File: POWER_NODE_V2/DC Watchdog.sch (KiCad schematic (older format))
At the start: 0 parts

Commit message: Power Node V2 WIP
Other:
- note added: "TODO: Connector, ESD protection"
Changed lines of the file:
@@
 Text HLabel 3200 2800 0    60   Input ~ 0
 DC_WATCHDOG
+Text Notes 4850 2750 0    60   ~ 0
+TODO: Connector, ESD protection
 $EndSCHEMATC

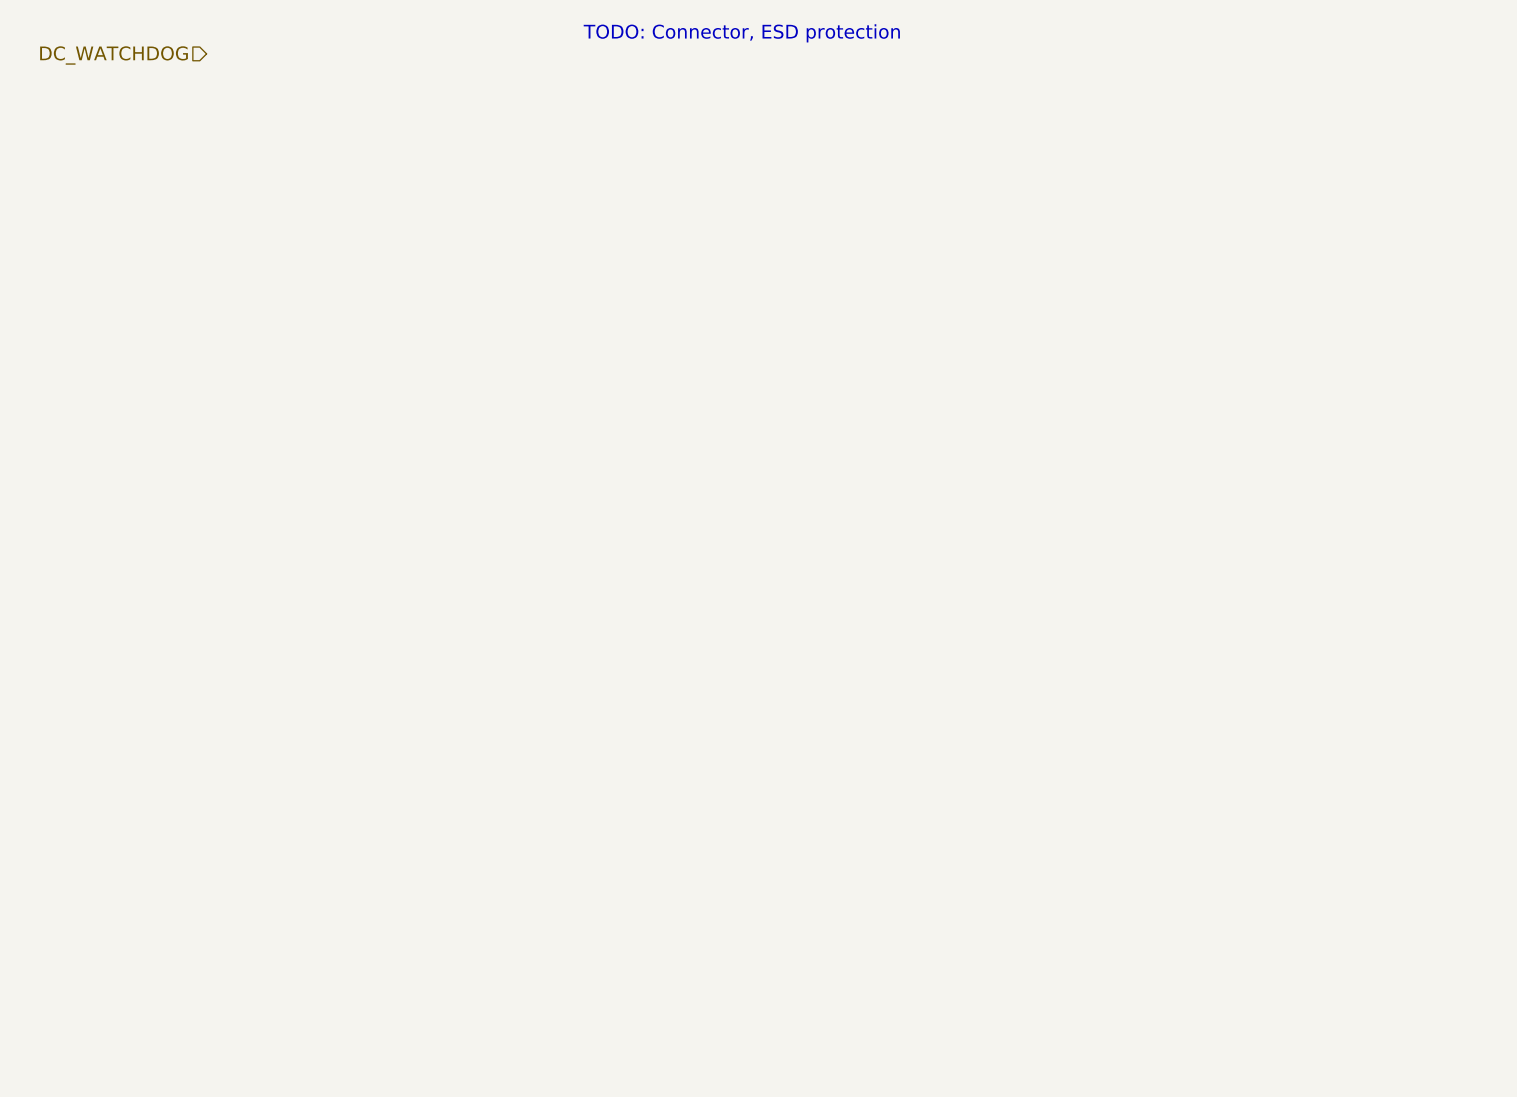
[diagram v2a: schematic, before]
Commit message: Schematic for Power Node V2 mostly done - mostly need connectors
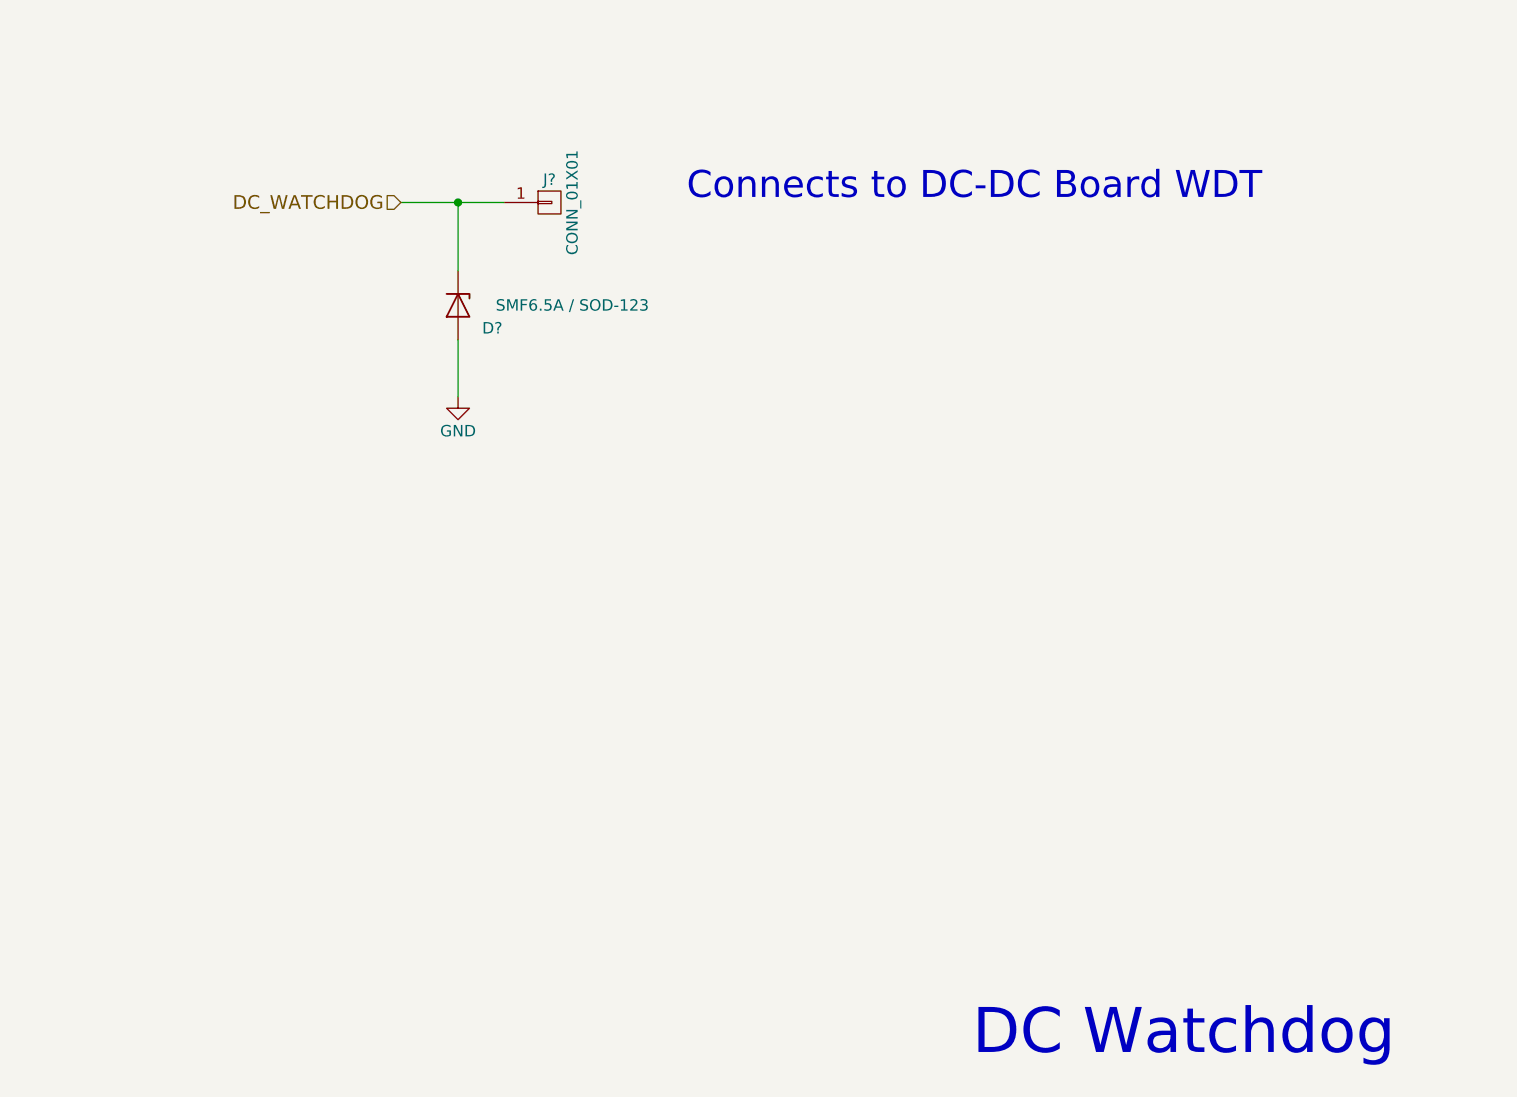
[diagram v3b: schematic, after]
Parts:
- added D?: SMF6.5A / SOD-123, symbol D_Zener
- added J?: CONN_01X01, symbol CONN_01X01
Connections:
- net DC_WATCHDOG: now also D?.1 (K), J?.1 (P1)
- new net GND: D?.2 (A)
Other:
- note added: "Connects to DC-DC Board WDT"
- note added: "DC Watchdog"
- note removed: "TODO: Connector, ESD protection"
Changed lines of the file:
@@
 EELAYER 25 0
 EELAYER END
-$Descr A4 11693 8268
+$Descr USLetter 11000 8500
 encoding utf-8
-Sheet 6 8
+Sheet 6 9
 Title ""
 Date ""
@@
 Comment4 ""
 $EndDescr
-Text HLabel 3200 2800 0    60   Input ~ 0
+Text HLabel 4050 3450 0    60   Input ~ 0
 DC_WATCHDOG
-Text Notes 4850 2750 0    60   ~ 0
-TODO: Connector, ESD protection
+$Comp
+L CONN_01X01 J?
+U 1 1 5951AEA4
+P 4700 3450
+F 0 "J?" H 4700 3550 50  0000 C CNN
+F 1 "CONN_01X01" V 4800 3450 50  0000 C CNN
+F 2 "" H 4700 3450 50  0001 C CNN
+F 3 "" H 4700 3450 50  0001 C CNN
+	1    4700 3450
+	1    0    0    -1
+$EndComp
+Wire Wire Line
+	4050 3450 4500 3450
+$Comp
+L D_Zener D?
+U 1 1 5952660A
+P 4300 3900
+F 0 "D?" V 4400 4050 50  0000 C CNN
+F 1 "SMF6.5A / SOD-123" V 4300 4400 50  0000 C CNN
+F 2 "" H 4300 3900 50  0001 C CNN
+F 3 "" H 4300 3900 50  0001 C CNN
+	1    4300 3900
+	0    1    1    0
+$EndComp
+Wire Wire Line
+	4300 3750 4300 3450
+Connection ~ 4300 3450
+$Comp
+L GND #PWR?
+U 1 1 5952668C
+P 4300 4300
+F 0 "#PWR?" H 4300 4050 50  0001 C CNN
+F 1 "GND" H 4300 4150 50  0000 C CNN
+F 2 "" H 4300 4300 50  0001 C CNN
+F 3 "" H 4300 4300 50  0001 C CNN
+	1    4300 4300
+	1    0    0    -1
+$EndComp
+Wire Wire Line
+	4300 4300 4300 4050
+Text Notes 5300 3450 0    118  ~ 0
+Connects to DC-DC Board WDT
+Text Notes 6550 7200 0    197  ~ 0
+DC Watchdog
 $EndSCHEMATC

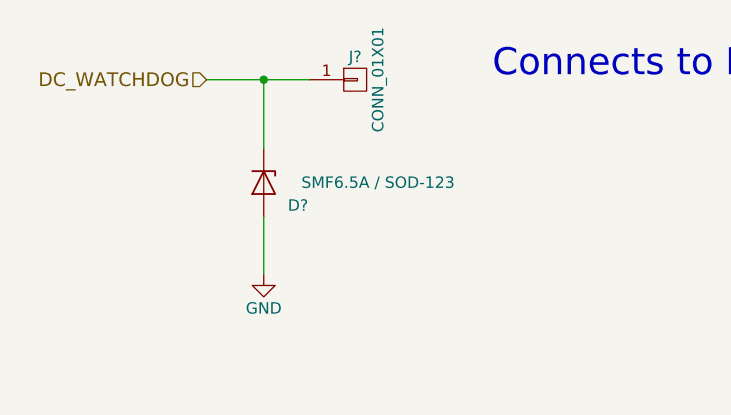
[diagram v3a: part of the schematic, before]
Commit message: made a lot of footprints, began PCB layout for power node v2
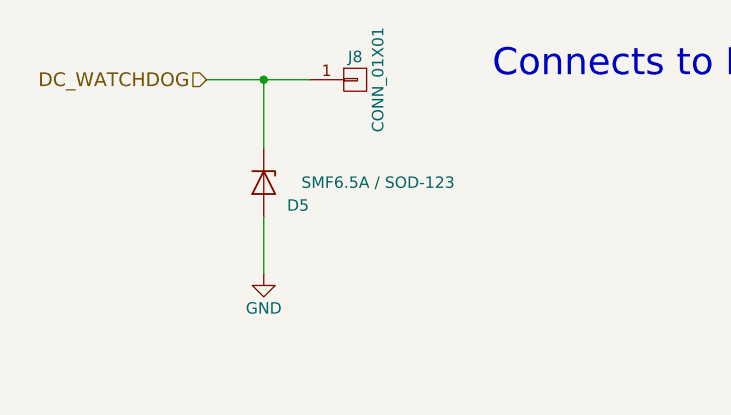
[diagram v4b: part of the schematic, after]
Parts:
- D5: renamed from D?; footprint (none) -> Diodes_SMD:D_SOD-123
- J8: renamed from J?; footprint (none) -> Pin_Headers:Pin_Header_Straight_1x01_Pitch2.54mm
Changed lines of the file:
@@
 DC_WATCHDOG
 $Comp
-L CONN_01X01 J?
+L CONN_01X01 J8
 U 1 1 5951AEA4
 P 4700 3450
-F 0 "J?" H 4700 3550 50  0000 C CNN
+F 0 "J8" H 4700 3550 50  0000 C CNN
 F 1 "CONN_01X01" V 4800 3450 50  0000 C CNN
-F 2 "" H 4700 3450 50  0001 C CNN
+F 2 "Pin_Headers:Pin_Header_Straight_1x01_Pitch2.54mm" H 4700 3450 50  0001 C CNN
 F 3 "" H 4700 3450 50  0001 C CNN
 	1    4700 3450
@@
 	4050 3450 4500 3450
 $Comp
-L D_Zener D?
+L D_Zener D5
 U 1 1 5952660A
 P 4300 3900
-F 0 "D?" V 4400 4050 50  0000 C CNN
+F 0 "D5" V 4400 4050 50  0000 C CNN
 F 1 "SMF6.5A / SOD-123" V 4300 4400 50  0000 C CNN
-F 2 "" H 4300 3900 50  0001 C CNN
+F 2 "Diodes_SMD:D_SOD-123" H 4300 3900 50  0001 C CNN
 F 3 "" H 4300 3900 50  0001 C CNN
 	1    4300 3900
@@
 Connection ~ 4300 3450
 $Comp
-L GND #PWR?
+L GND #PWR096
 U 1 1 5952668C
 P 4300 4300
-F 0 "#PWR?" H 4300 4050 50  0001 C CNN
+F 0 "#PWR096" H 4300 4050 50  0001 C CNN
 F 1 "GND" H 4300 4150 50  0000 C CNN
 F 2 "" H 4300 4300 50  0001 C CNN

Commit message: All modelled, schematics and mechanical just need a double check
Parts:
- removed J8: CONN_01X01, Pin_Headers:Pin_Header_Straight_1x01_Pitch2.54mm, symbol CONN_01X01
- added J8: 3-641215-3, rLoop_Footprints:3-641215-3_3Pin_Latching_Header, symbol CONN_01X03
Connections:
- net DC_WATCHDOG: now also J8.1 (P1), J8.2 (P2), J8.3 (P3)
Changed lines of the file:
@@
 Text HLabel 4050 3450 0    60   Input ~ 0
 DC_WATCHDOG
-$Comp
-L CONN_01X01 J8
-U 1 1 5951AEA4
-P 4700 3450
-F 0 "J8" H 4700 3550 50  0000 C CNN
-F 1 "CONN_01X01" V 4800 3450 50  0000 C CNN
-F 2 "Pin_Headers:Pin_Header_Straight_1x01_Pitch2.54mm" H 4700 3450 50  0001 C CNN
-F 3 "" H 4700 3450 50  0001 C CNN
-	1    4700 3450
-	1    0    0    -1
-$EndComp
 Wire Wire Line
 	4050 3450 4500 3450
@@
 Connection ~ 4300 3450
 $Comp
-L GND #PWR096
+L GND #PWR095
 U 1 1 5952668C
 P 4300 4300
-F 0 "#PWR096" H 4300 4050 50  0001 C CNN
+F 0 "#PWR095" H 4300 4050 50  0001 C CNN
 F 1 "GND" H 4300 4150 50  0000 C CNN
 F 2 "" H 4300 4300 50  0001 C CNN
@@
 Wire Wire Line
 	4300 4300 4300 4050
-Text Notes 5300 3450 0    118  ~ 0
+Text Notes 5100 3450 0    118  ~ 0
 Connects to DC-DC Board WDT
 Text Notes 6550 7200 0    197  ~ 0
 DC Watchdog
+$Comp
+L CONN_01X03 J8
+U 1 1 595ADFEE
+P 4700 3550
+F 0 "J8" H 4700 3750 50  0000 C CNN
+F 1 "3-641215-3" V 4800 3550 50  0000 C CNN
+F 2 "rLoop_Footprints:3-641215-3_3Pin_Latching_Header" H 4700 3550 50  0001 C CNN
+F 3 "" H 4700 3550 50  0001 C CNN
+	1    4700 3550
+	1    0    0    -1
+$EndComp
+Wire Wire Line
+	4500 3450 4500 3650
+Connection ~ 4500 3550
 $EndSCHEMATC
